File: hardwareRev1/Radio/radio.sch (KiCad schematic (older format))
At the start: 53 parts, among them J1 edgeMountSMA, J2 edgeMountSMA, P1 CONN_11X2, P2 CONN_1, P3 CONN_8, P4 CONN_5X2, P5 CONN_1, P6 CONN_1, U1 AX503, U2 PE42424, U4 MKL26Z128VLH4, U6 MICRO-B_USB, X1 TCXO

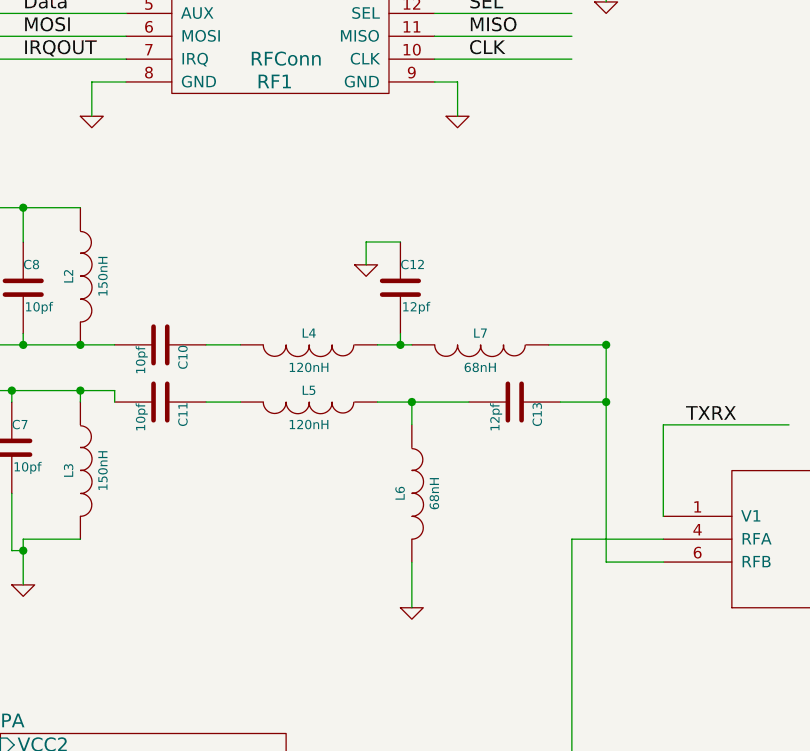
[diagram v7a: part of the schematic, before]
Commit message: Modified the radio according to John. Should be almost good to go.
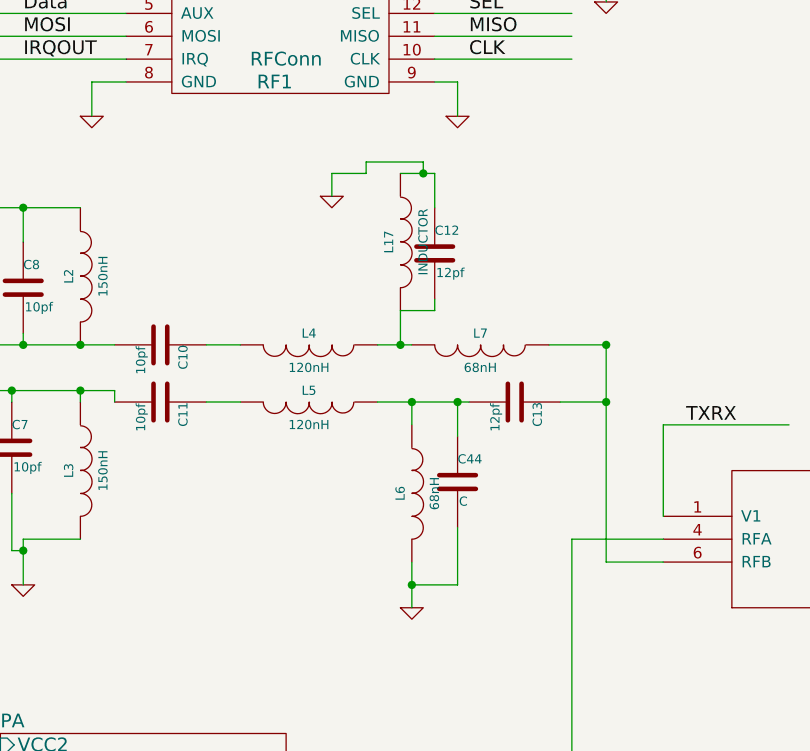
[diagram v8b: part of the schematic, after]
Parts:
- added C44: C, Capacitors_SMD:C_0402, symbol C
- added L17: INDUCTOR, Resistors_SMD:R_0402, symbol INDUCTOR
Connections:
- wire segments 301 -> 311
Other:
- moved on the sheet: C12
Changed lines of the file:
@@
 L C C12
 U 1 1 55504B79
-P 5950 3300
-F 0 "C12" H 5950 3400 40  0000 L CNN
-F 1 "12pf" H 5956 3215 40  0000 L CNN
-F 2 "Capacitors_SMD:C_0402" H 5988 3150 30  0001 C CNN
-F 3 "" H 5950 3300 60  0000 C CNN
-	1    5950 3300
+P 6100 3150
+F 0 "C12" H 6100 3250 40  0000 L CNN
+F 1 "12pf" H 6106 3065 40  0000 L CNN
+F 2 "Capacitors_SMD:C_0402" H 6138 3000 30  0001 C CNN
+F 3 "" H 6100 3150 60  0000 C CNN
+	1    6100 3150
 	1    0    0    -1
 $EndComp
@@
 L GND #PWR03
 U 1 1 55504EED
-P 5800 3200
-F 0 "#PWR03" H 5800 3200 30  0001 C CNN
-F 1 "GND" H 5800 3130 30  0001 C CNN
-F 2 "" H 5800 3200 60  0000 C CNN
-F 3 "" H 5800 3200 60  0000 C CNN
-	1    5800 3200
+P 5650 2900
+F 0 "#PWR03" H 5650 2900 30  0001 C CNN
+F 1 "GND" H 5650 2830 30  0001 C CNN
+F 2 "" H 5650 2900 60  0000 C CNN
+F 3 "" H 5650 2900 60  0000 C CNN
+	1    5650 2900
 	1    0    0    -1
 $EndComp
@@
 	5850 3550 6000 3550
 Wire Wire Line
-	5950 3550 5950 3500
+	5950 3400 5950 3550
 Connection ~ 5950 3550
 Wire Wire Line
@@
 	6000 4500 6000 4700
 Wire Wire Line
-	5950 3100 5800 3100
-Wire Wire Line
-	5800 3100 5800 3200
+	5800 2800 5650 2800
+Wire Wire Line
+	5650 2800 5650 2900
 Wire Wire Line
 	6850 3800 6650 3800
@@
 	1    0    0    -1
 $EndComp
+$Comp
+L C C44
+U 1 1 55F65115
+P 6200 4150
+F 0 "C44" H 6200 4250 40  0000 L CNN
+F 1 "C" H 6206 4065 40  0000 L CNN
+F 2 "Capacitors_SMD:C_0402" H 6238 4000 30  0001 C CNN
+F 3 "" H 6200 4150 60  0000 C CNN
+	1    6200 4150
+	1    0    0    -1
+$EndComp
+$Comp
+L INDUCTOR L17
+U 1 1 55F6516E
+P 5950 3100
+F 0 "L17" V 5900 3100 40  0000 C CNN
+F 1 "INDUCTOR" V 6050 3100 40  0000 C CNN
+F 2 "Resistors_SMD:R_0402" H 5950 3100 60  0001 C CNN
+F 3 "" H 5950 3100 60  0000 C CNN
+	1    5950 3100
+	1    0    0    -1
+$EndComp
+Wire Wire Line
+	6200 3950 6200 3800
+Connection ~ 6200 3800
+Wire Wire Line
+	6200 4350 6200 4600
+Wire Wire Line
+	6200 4600 6000 4600
+Connection ~ 6000 4600
+Wire Wire Line
+	5950 3400 6100 3400
+Wire Wire Line
+	6100 3400 6100 3350
+Wire Wire Line
+	6100 2950 6100 2800
+Wire Wire Line
+	6100 2800 5950 2800
+Wire Wire Line
+	5800 2800 5800 2750
+Wire Wire Line
+	5800 2750 6050 2750
+Wire Wire Line
+	6050 2750 6050 2800
+Connection ~ 6050 2800
 $EndSCHEMATC
